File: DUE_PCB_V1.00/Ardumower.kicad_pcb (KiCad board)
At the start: 2 copper layers, 169.9 x 97 mm, 81 parts, among them J1 9V IN, J10 Sonar_R, J11 Sonar_C, J12 Sonar_L, J13 P_Right, J14 Buzzer, J15 Button, J16 US1, J17 US2, J18 US3, J19 P_Left, J2 I2C0_1, J20 Remote, J21 PCB_2, J22 Ser0, J23 Ser1, J24 Ser2, J25 5V IN, J26 Cutter1, J27 MotorR, J28 MotorL, J29 3.3V IN, J3 I2C0_2, J30 I2C1_2, J31 Ser3, J32 24V In, J33 ReserveD8, J34 ReserveD9, J35 ReserveD49, J36 ReserveA10, J37 RPM_Mow, J38 ODO_Left, J39 ODO_Right, J4 I2C1_1, J5 Bumper, J6 Drop_Left, J7 Drop_Right, J8 Tilt, J9 Rain, U1 MC33926, U2 MC33926

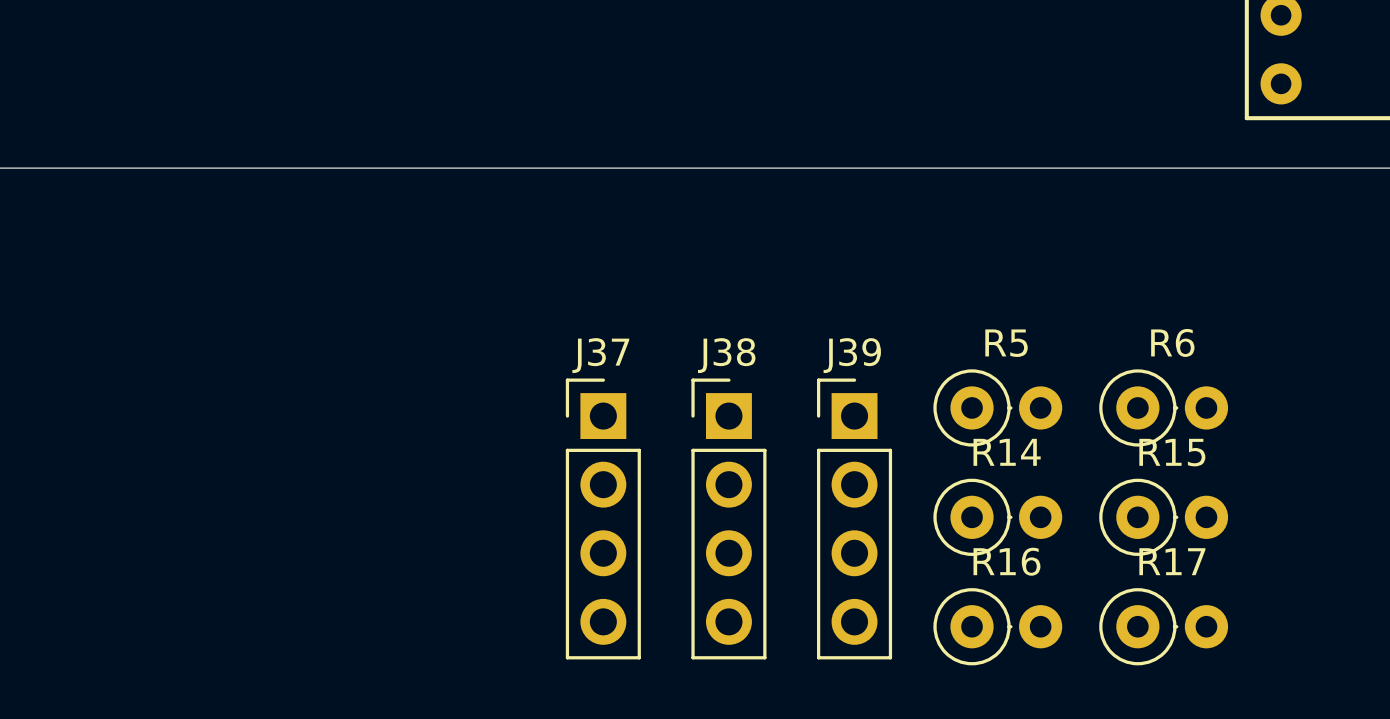
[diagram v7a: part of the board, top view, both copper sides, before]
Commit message: Add Voltage Divider
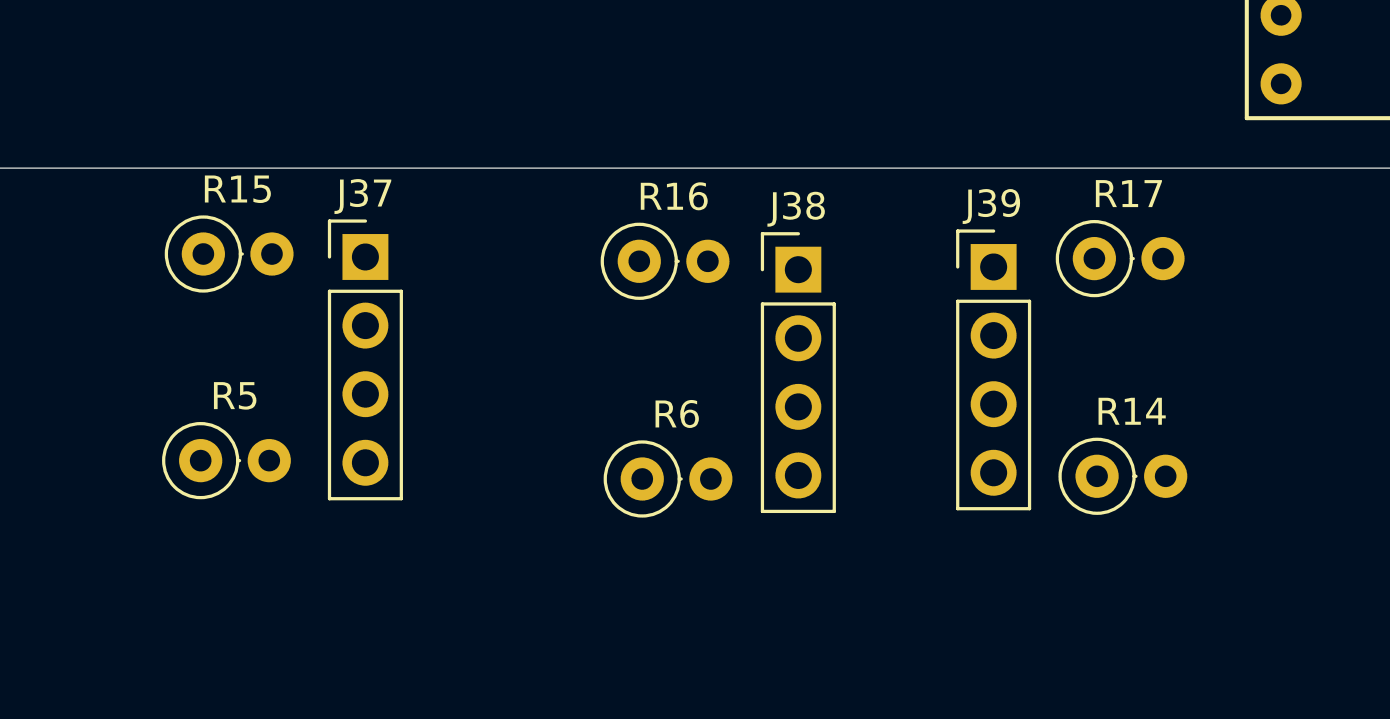
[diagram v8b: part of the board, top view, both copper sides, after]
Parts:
- moved R15 35.9 mm to (131.1, 134.8)
- moved R5 28.6 mm to (131.0, 142.4)
- moved R6 18.5 mm to (147.3, 143.1)
- moved R16 18.3 mm to (147.2, 135.1)
- moved R17 13.7 mm to (164.1, 135.0)
- moved J37 10.6 mm to (137.1, 134.9)
- moved J39 7.55 mm to (160.3, 135.3)
- moved J38 6.00 mm to (153.1, 135.4)
- moved R14 4.87 mm to (164.2, 143.0)
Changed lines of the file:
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@@
   )
   (module Resistor_THT:R_Axial_DIN0207_L6.3mm_D2.5mm_P2.54mm_Vertical (layer F.Cu)
-    (at 165.67 148.6)
+    (at 164.06 134.97)
     (descr "Resistor, Axial_DIN0207 series, Axial, Vertical, pin pitch=2.54mm, 0.25W = 1/4W, length*diameter=6.3*2.5mm^2, http://cdn-reichelt.de/documents/datenblatt/B400/1_4W%23YAG.pdf")
     (tags "Resistor Axial_DIN0207 series Axial Vertical pin pitch 2.54mm 0.25W = 1/4W length 6.3mm diameter 2.5mm")
@@
   )
   (module Resistor_THT:R_Axial_DIN0207_L6.3mm_D2.5mm_P2.54mm_Vertical (layer F.Cu)
-    (at 159.53 148.6)
+    (at 147.21 135.07)
     (descr "Resistor, Axial_DIN0207 series, Axial, Vertical, pin pitch=2.54mm, 0.25W = 1/4W, length*diameter=6.3*2.5mm^2, http://cdn-reichelt.de/documents/datenblatt/B400/1_4W%23YAG.pdf")
     (tags "Resistor Axial_DIN0207 series Axial Vertical pin pitch 2.54mm 0.25W = 1/4W length 6.3mm diameter 2.5mm")
@@
   )
   (module Resistor_THT:R_Axial_DIN0207_L6.3mm_D2.5mm_P2.54mm_Vertical (layer F.Cu)
-    (at 165.67 144.55)
+    (at 131.07 134.8)
     (descr "Resistor, Axial_DIN0207 series, Axial, Vertical, pin pitch=2.54mm, 0.25W = 1/4W, length*diameter=6.3*2.5mm^2, http://cdn-reichelt.de/documents/datenblatt/B400/1_4W%23YAG.pdf")
     (tags "Resistor Axial_DIN0207 series Axial Vertical pin pitch 2.54mm 0.25W = 1/4W length 6.3mm diameter 2.5mm")
@@
   )
   (module Resistor_THT:R_Axial_DIN0207_L6.3mm_D2.5mm_P2.54mm_Vertical (layer F.Cu)
-    (at 159.53 144.55)
+    (at 164.16 143.03)
     (descr "Resistor, Axial_DIN0207 series, Axial, Vertical, pin pitch=2.54mm, 0.25W = 1/4W, length*diameter=6.3*2.5mm^2, http://cdn-reichelt.de/documents/datenblatt/B400/1_4W%23YAG.pdf")
     (tags "Resistor Axial_DIN0207 series Axial Vertical pin pitch 2.54mm 0.25W = 1/4W length 6.3mm diameter 2.5mm")
@@
   )
   (module Resistor_THT:R_Axial_DIN0207_L6.3mm_D2.5mm_P2.54mm_Vertical (layer F.Cu)
-    (at 165.67 140.5)
+    (at 147.32 143.13)
     (descr "Resistor, Axial_DIN0207 series, Axial, Vertical, pin pitch=2.54mm, 0.25W = 1/4W, length*diameter=6.3*2.5mm^2, http://cdn-reichelt.de/documents/datenblatt/B400/1_4W%23YAG.pdf")
     (tags "Resistor Axial_DIN0207 series Axial Vertical pin pitch 2.54mm 0.25W = 1/4W length 6.3mm diameter 2.5mm")
@@
   )
   (module Resistor_THT:R_Axial_DIN0207_L6.3mm_D2.5mm_P2.54mm_Vertical (layer F.Cu)
-    (at 159.53 140.5)
+    (at 130.97 142.45)
     (descr "Resistor, Axial_DIN0207 series, Axial, Vertical, pin pitch=2.54mm, 0.25W = 1/4W, length*diameter=6.3*2.5mm^2, http://cdn-reichelt.de/documents/datenblatt/B400/1_4W%23YAG.pdf")
     (tags "Resistor Axial_DIN0207 series Axial Vertical pin pitch 2.54mm 0.25W = 1/4W length 6.3mm diameter 2.5mm")
@@
   )
   (module Connector_PinHeader_2.54mm:PinHeader_1x04_P2.54mm_Vertical (layer F.Cu)
-    (at 155.18 140.8)
+    (at 160.33 135.28)
     (descr "Through hole straight pin header, 1x04, 2.54mm pitch, single row")
     (tags "Through hole pin header THT 1x04 2.54mm single row")
@@
   )
   (module Connector_PinHeader_2.54mm:PinHeader_1x04_P2.54mm_Vertical (layer F.Cu)
-    (at 150.53 140.8)
+    (at 153.1 135.38)
     (descr "Through hole straight pin header, 1x04, 2.54mm pitch, single row")
     (tags "Through hole pin header THT 1x04 2.54mm single row")
@@
   )
   (module Connector_PinHeader_2.54mm:PinHeader_1x04_P2.54mm_Vertical (layer F.Cu)
-    (at 145.88 140.8)
+    (at 137.07 134.91)
     (descr "Through hole straight pin header, 1x04, 2.54mm pitch, single row")
     (tags "Through hole pin header THT 1x04 2.54mm single row")
